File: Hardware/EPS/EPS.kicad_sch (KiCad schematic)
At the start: 1 part

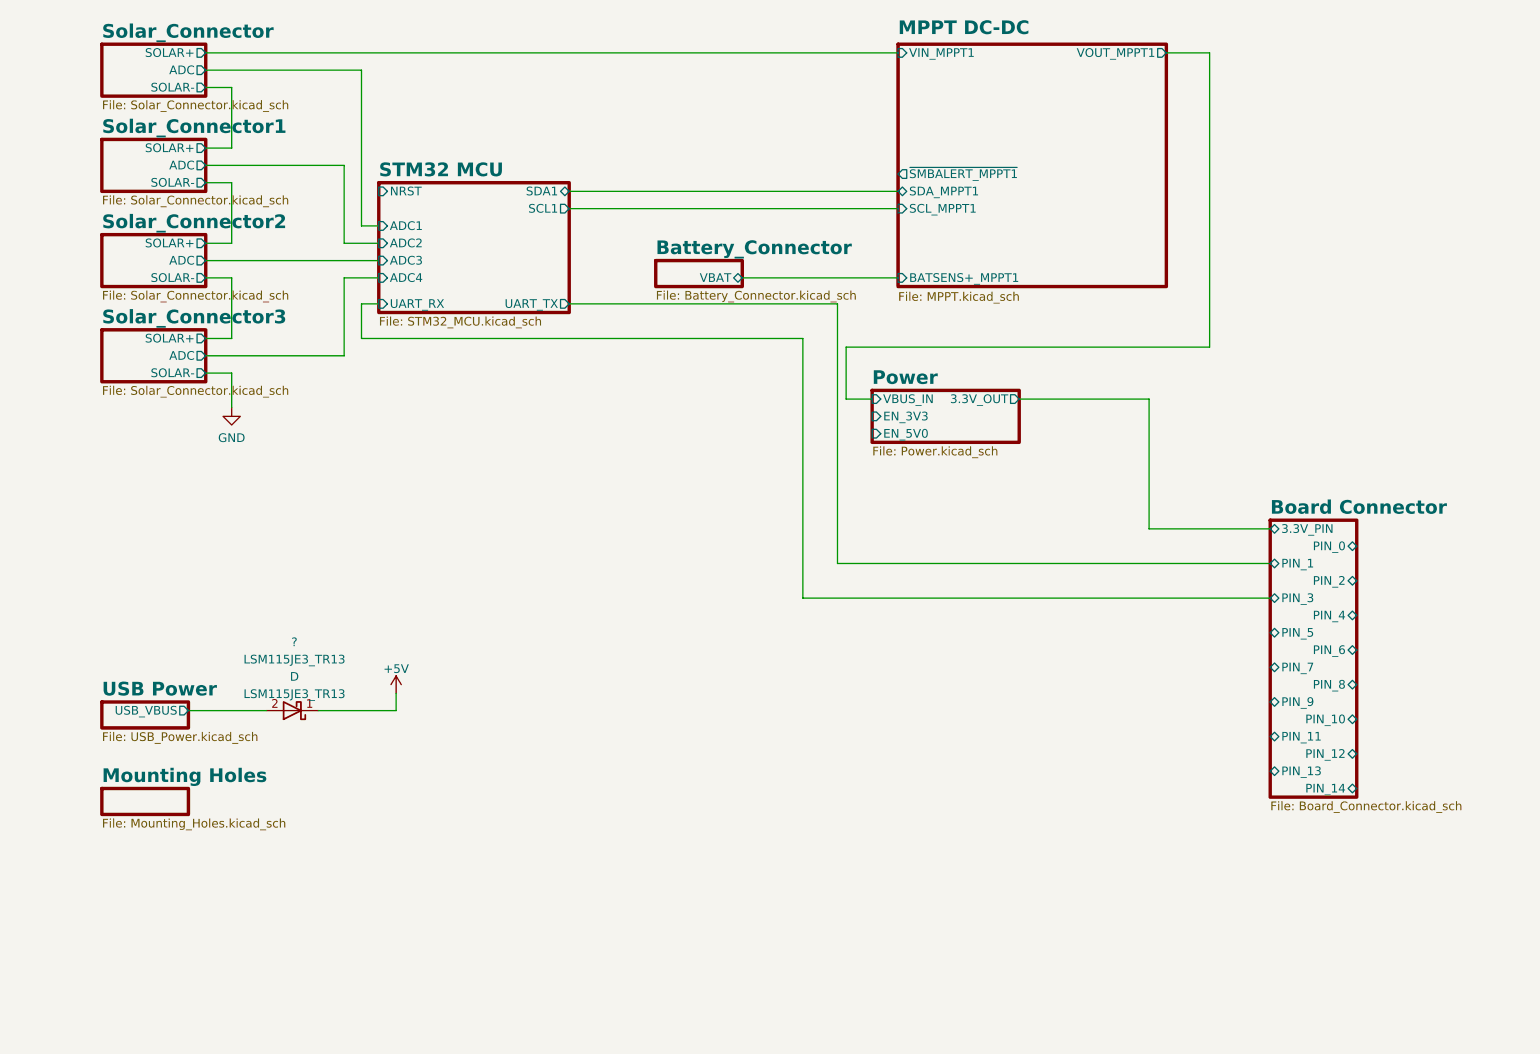
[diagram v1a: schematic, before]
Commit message: Defined pinout for board connector, major revision
v0.0.3 - Fixed erratas and cleaned the schematic
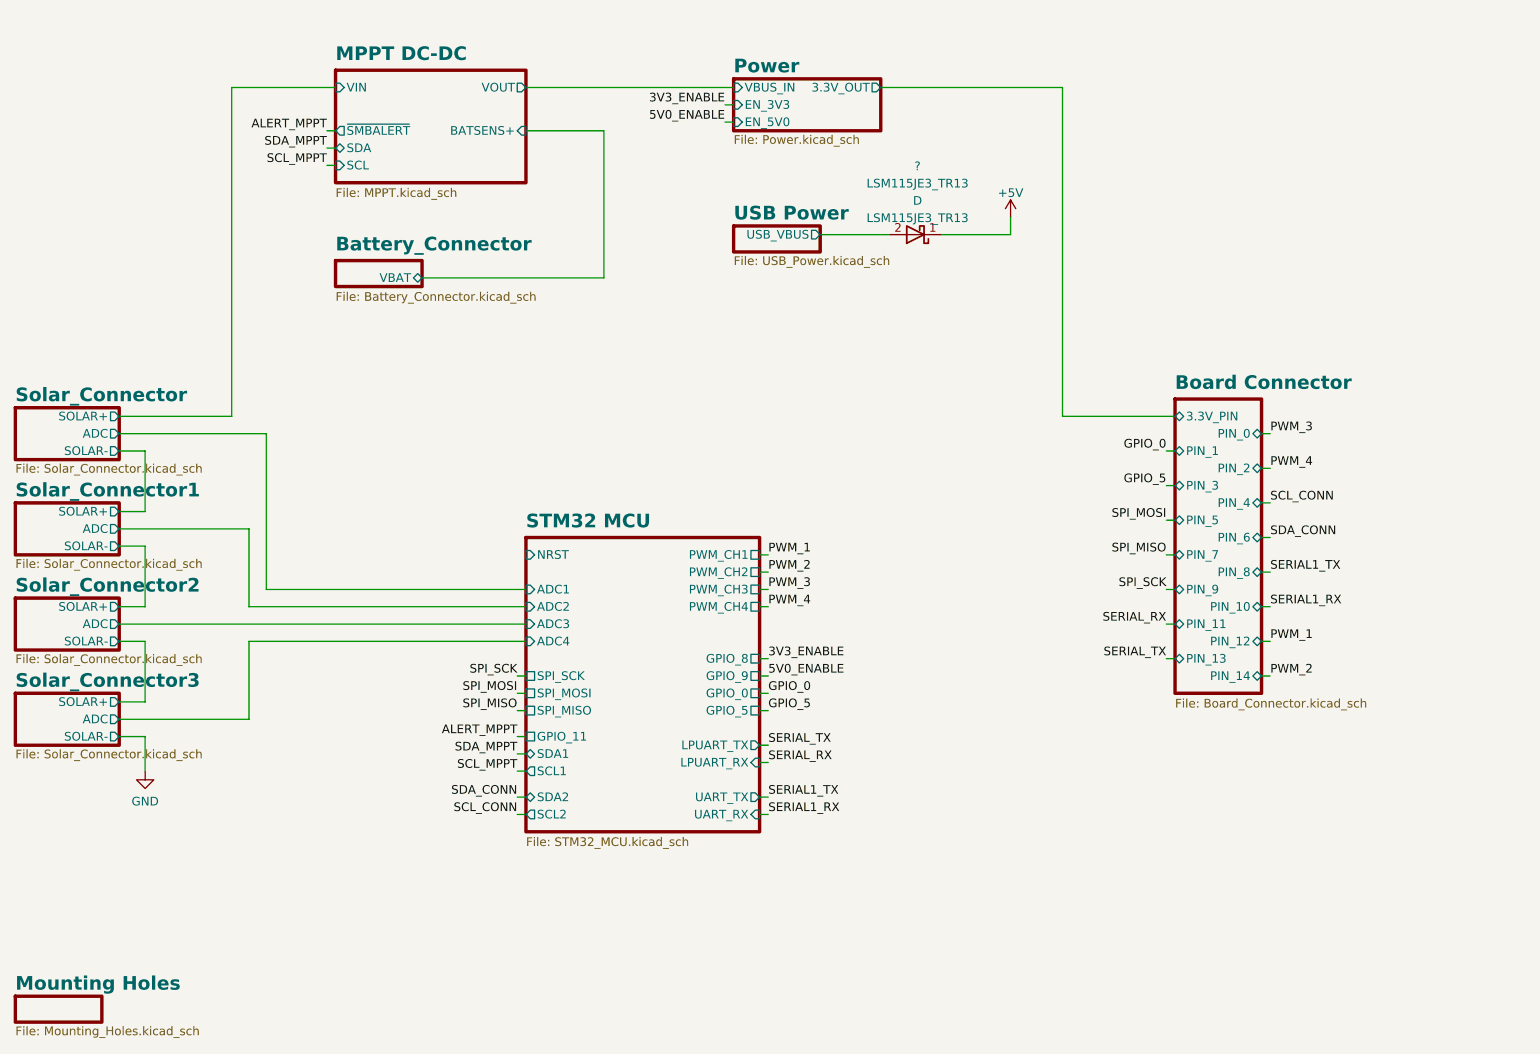
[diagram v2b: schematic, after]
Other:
- sheet MPPT DC-DC ports: added BATSENS+, SCL, SDA, VIN, VOUT, ~{SMBALERT}; removed BATSENS+_MPPT1, SCL_MPPT1, SDA_MPPT1, VIN_MPPT1, VOUT_MPPT1, ~{SMBALERT_MPPT1}
- sheet STM32 MCU ports: added GPIO_0, GPIO_11, GPIO_5, GPIO_8, GPIO_9, LPUART_RX, LPUART_TX, PWM_CH1, PWM_CH2, PWM_CH3, PWM_CH4, SCL2, SDA2, SPI_MISO, SPI_MOSI, SPI_SCK; removed none
- moved on the sheet: ?
